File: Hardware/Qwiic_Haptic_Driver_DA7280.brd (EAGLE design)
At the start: 25.4 x 25.4 mm, 21 parts, among them J1 QWIIC_RIGHT_ANGLE, J2 QWIIC_RIGHT_ANGLE

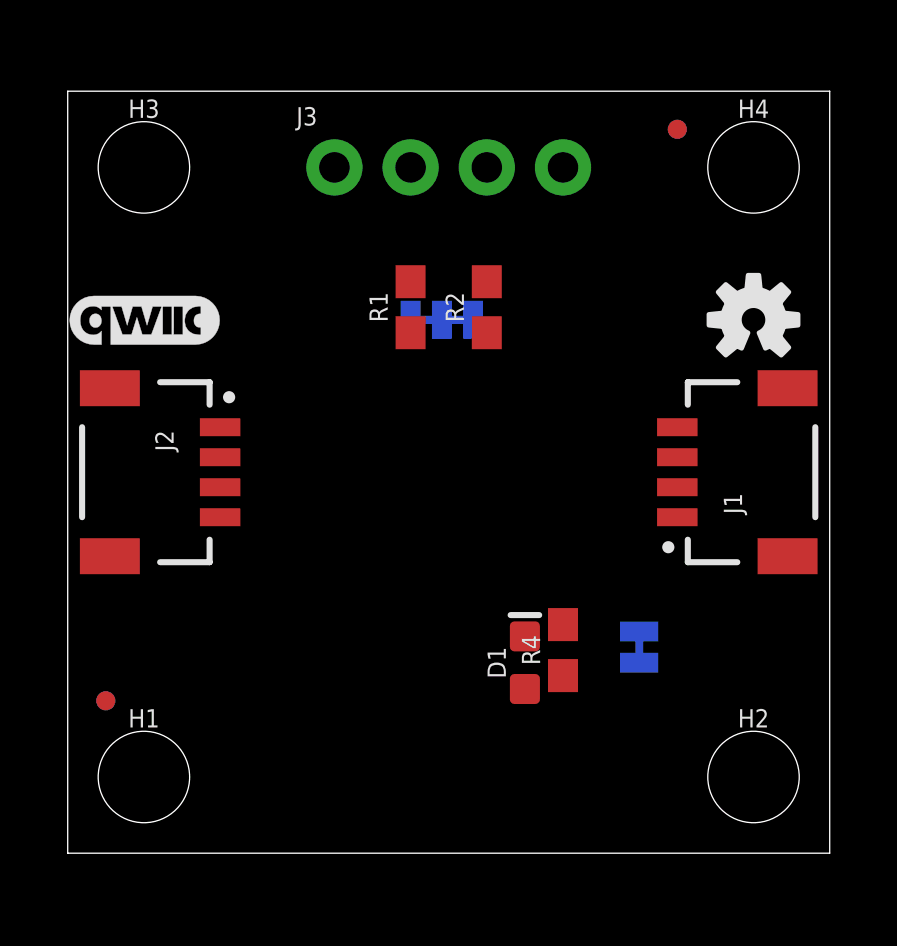
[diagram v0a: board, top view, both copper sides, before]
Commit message: Fully routed the board - still needs silk
Minor changes to the DA7280:
* symbol size was shortened.
* Footprint was centered at 0,0
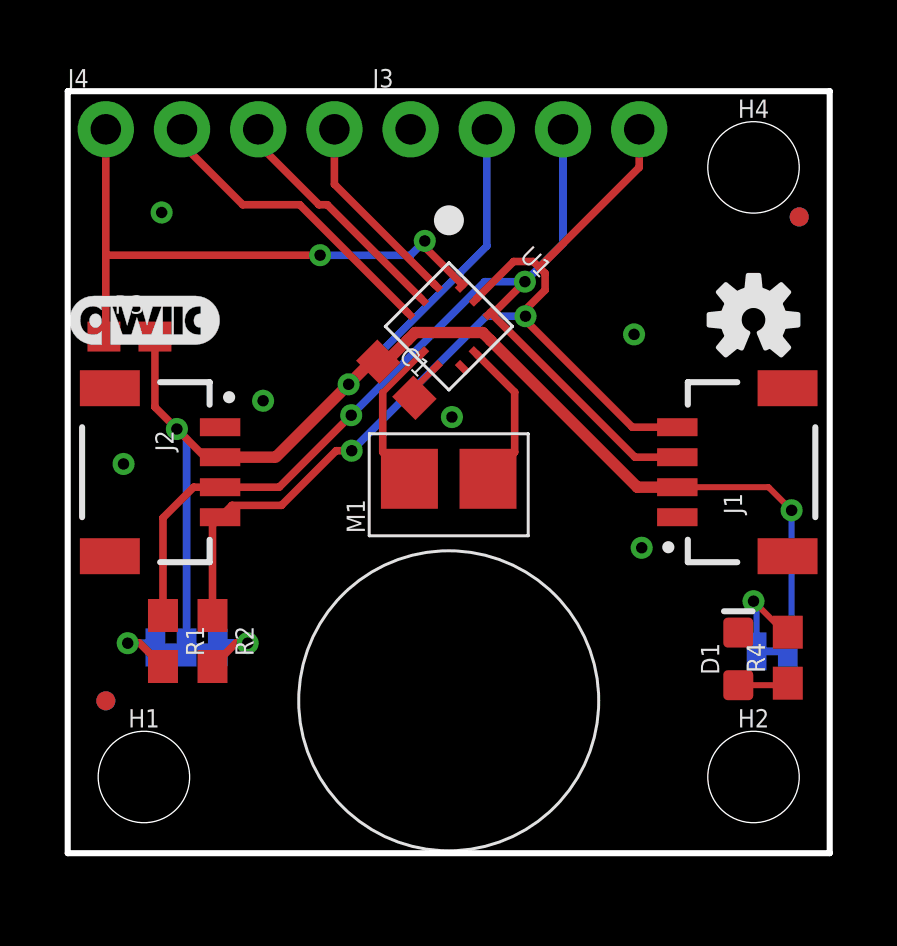
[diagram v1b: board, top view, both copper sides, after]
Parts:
- removed H3: STAND-OFFTIGHT, SparkFun-Hardware:STAND-OFF-TIGHT
- added C1: 0.1uF, SparkFun-Capacitors:0603
- added J4: (no value), SparkFun-Connectors:1X04_NO_SILK
- added M1: G1040003D_COIN_VIBRATION_MOTOR, TEMP:COIN_VIBRATION_MOTOR
- added R3: 10k, SparkFun-Resistors:0603
- added U1: HAPTIC_DRIVER_DA7280, TEMP:QFN_DA7280
- moved R2 14.4 mm to (4.83, 7.07), turned to 270 degrees
- moved R1 13.9 mm to (3.17, 7.07), turned to 270 degrees
- moved JP3 13.8 mm to (3.96, 6.86)
- moved R4 7.50 mm to (24.0, 6.52)
- moved D1 7.11 mm to (22.4, 6.48)
- moved FD1 5.00 mm to (24.4, 21.2)
- moved FD2 5.00 mm to (24.4, 21.2)
- moved JP1 4.43 mm to (23.5, 6.73), turned to 180 degrees
- moved J3 2.84 mm to (11.4, 24.1)
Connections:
- new net !INT!: J4.1, R3.1, U1.P12
- new net GPI0/PWM: J4.2, U1.P3
- new net GPI1: J4.3, U1.P2
- new net GPI2: J4.4, U1.P1
- new net N$5: M1.P$2, U1.P5
- new net N$6: M1.P$1, U1.P8
- net 3.3V: now also C1.1, R3.2, U1.P4, U1.P9
- net GND: now also C1.2, U1.P6, U1.P7
- net SCL: now also U1.P11
- net SDA: now also U1.P10
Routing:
- net 3.3V: track 0.00 -> 51.0 mm, vias 0 -> 3
- net SDA: track 0.00 -> 34.0 mm, vias 0 -> 2
- net SCL: track 0.00 -> 33.7 mm, vias 0 -> 2
- net !INT!: track 0.00 -> 19.8 mm, vias 0 -> 2
- net GPI0/PWM: track 0.00 -> 10.3 mm
- net GPI1: track 0.00 -> 8.07 mm
- net GPI2: track 0.00 -> 6.58 mm
- net N$5: track 0.00 -> 5.06 mm
- net N$6: track 0.00 -> 5.06 mm
- net N$2: track 0.00 -> 3.28 mm, vias 0 -> 1
- net N$4: track 0.00 -> 2.56 mm, vias 0 -> 1
- net N$3: track 0.00 -> 2.48 mm, vias 0 -> 1
- net N$1: track 0.00 -> 1.68 mm
- net GND: track 0.00 -> 1.29 mm, vias 0 -> 6
- added copper zone on layer 1, net GND
- added copper zone on layer 16, net GND

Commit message: Adds silk to PTH headers, cleans up schematic
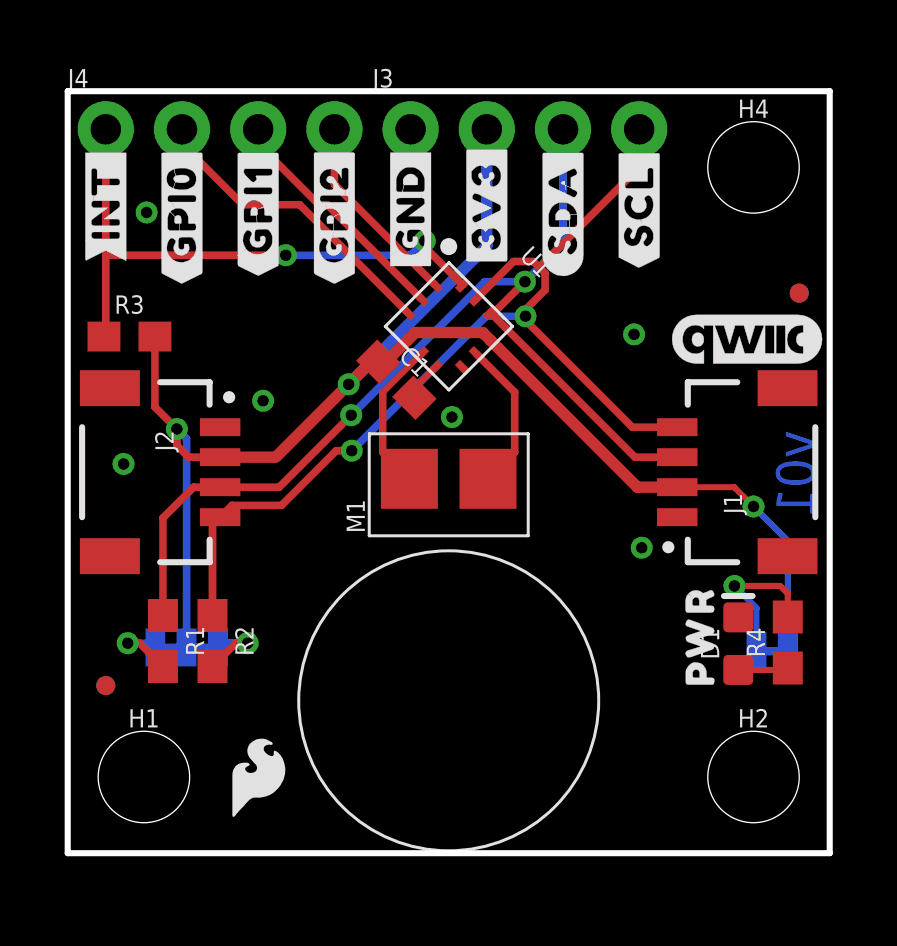
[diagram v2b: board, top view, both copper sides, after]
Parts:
- removed LOGO2: OSHW-LOGOS, SparkFun-Aesthetics:OSHW-LOGO-S
- added U$10: (no value), top:HAPTIC7
- added U$11: (no value), top:MOTOR_DRIVER8
- added U$12: (no value), bot:#GPI0#PWM#2
- added U$13: (no value), bot:#GPI1#2
- added U$14: (no value), bot:#GPI2#2
- added U$15: (no value), bot:#INT#3
- added U$16: (no value), bot:#SDA#0
- added U$17: (no value), SparkFun-Aesthetics:SFE_LOGO_FLAME_.1
- added U$18, U$3: (no value), top:#GND#0
- added U$19: (no value), top:#SCL#5
- added U$2, U$25: (no value), top:#3V3#1
- added U$20: (no value), top:PWR72810
- added U$21: (no value), bot:#SCL#1
- added U$22: (no value), SparkFun-Aesthetics:OSHW-LOGO-MINI
- added U$23: (no value), bot:#I2C#4
- added U$24: (no value), bot:#LED#4
- added U$4: (no value), top:#GPI0#6
- added U$5: (no value), top:#GPI1#6
- added U$6: (no value), top:#GPI2#6
- added U$7: (no value), top:#INT#6
- added U$8: (no value), top:#SDA#4
- added U$9: (no value), top:DA72809
- moved U$1 20.1 mm to (22.6, 17.1)
- moved FRAME1 5.68 mm to (-14.0, -12.7)
- moved FD1 2.54 mm to (24.4, 18.7)
- moved FD2 2.54 mm to (24.4, 18.7)
- moved LOGO1 2.36 mm to (15.0, 1.95)
- moved D1 0.51 mm to (22.4, 6.99)
- moved FD3 0.51 mm to (1.27, 5.59)
- moved FD4 0.51 mm to (1.27, 5.59)
- moved R4 0.51 mm to (24.0, 7.02)
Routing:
- net N$2: track 3.28 -> 5.15 mm
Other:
- board text added: "Elias Santistevan"
- board text added: "v01"

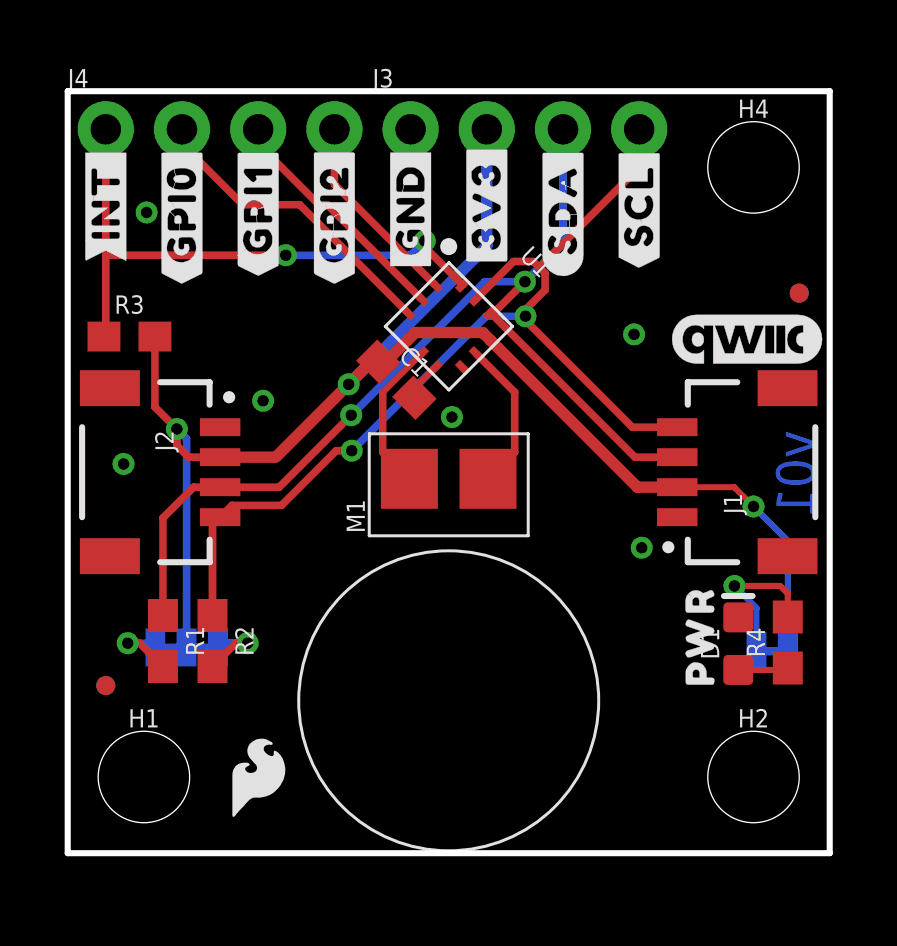
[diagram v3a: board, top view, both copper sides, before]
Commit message: Moves PTH interrupt closer to GND PTH hold and shifts all the GPI down.
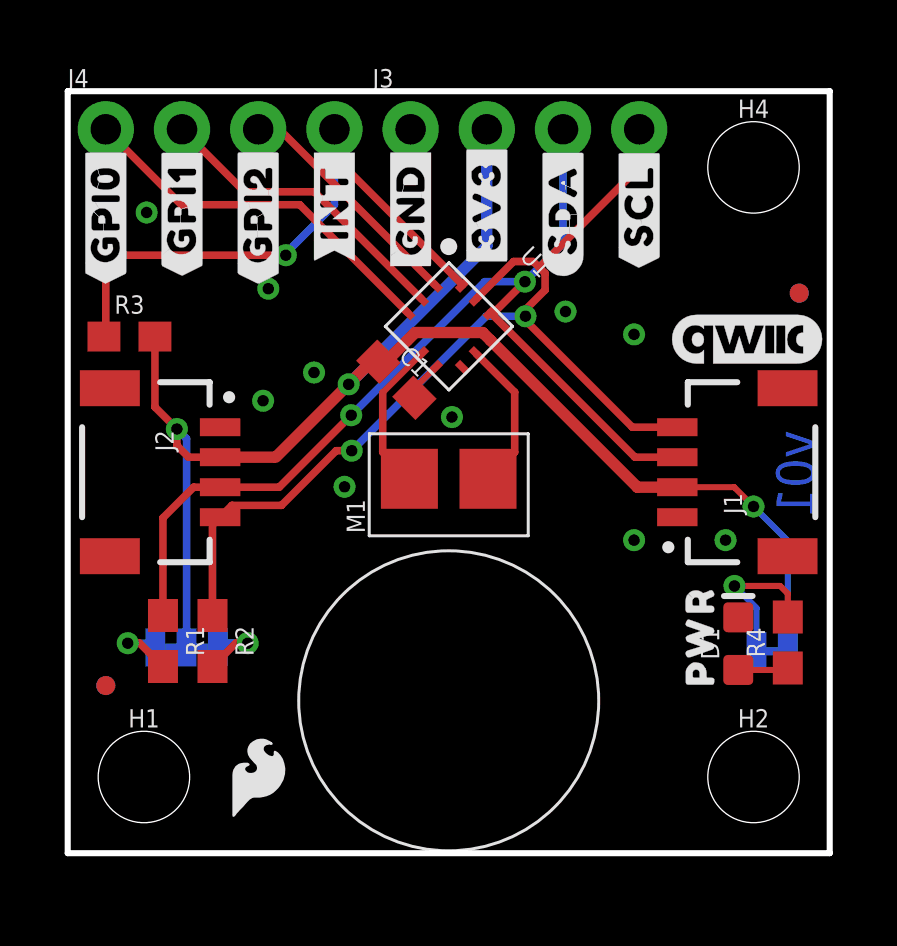
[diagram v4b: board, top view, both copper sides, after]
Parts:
- moved U$15 7.62 mm to (8.89, 21.7)
- moved U$7 7.62 mm to (8.89, 21.7)
- moved U$12 2.54 mm to (1.27, 19.1)
- moved U$14 2.54 mm to (6.35, 21.3)
- moved U$6 2.54 mm to (6.35, 21.3)
- moved U$4 2.54 mm to (1.27, 21.3)
- moved U$13 2.54 mm to (3.81, 21.5)
- moved U$5 2.54 mm to (3.81, 21.5)
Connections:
- net !INT!: now also J4.4; no longer J4.1
- net GPI0/PWM: now also J4.1; no longer J4.2
- net GPI1: now also J4.2; no longer J4.3
- net GPI2: now also J4.3; no longer J4.4
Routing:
- net GPI1: track 8.07 -> 10.3 mm
- net GPI0/PWM: track 10.3 -> 12.6 mm
- net GPI2: track 6.58 -> 8.05 mm
- net !INT!: track 19.8 -> 20.2 mm, vias 2 -> 1
- net GND: vias 6 -> 10
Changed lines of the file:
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@@
 <layer number="115" name="ReferenceISLANDS" color="7" fill="1" visible="no" active="no"/>
 <layer number="116" name="Patch_BOT" color="9" fill="4" visible="no" active="no"/>
-<layer number="117" name="PM_Ref" color="26" fill="1" visible="yes" active="yes"/>
+<layer number="117" name="PM_Ref" color="26" fill="1" visible="no" active="yes"/>
 <layer number="118" name="Rect_Pads" color="7" fill="1" visible="no" active="no"/>
-<layer number="119" name="PF_Ref" color="31" fill="1" visible="yes" active="yes"/>
-<layer number="120" name="WFL_Ref" color="25" fill="1" visible="yes" active="yes"/>
+<layer number="119" name="PF_Ref" color="31" fill="1" visible="no" active="yes"/>
+<layer number="120" name="WFL_Ref" color="25" fill="1" visible="no" active="yes"/>
 <layer number="121" name="_tsilk" color="7" fill="1" visible="no" active="no"/>
 <layer number="122" name="_bsilk" color="7" fill="1" visible="no" active="no"/>
@@
 </element>
 <element name="U$3" library="top" package="#GND#0" value="" x="11.43" y="21.463" smashed="yes" rot="R90"/>
-<element name="U$4" library="top" package="#GPI0#6" value="" x="3.81" y="21.336" smashed="yes" rot="R90"/>
-<element name="U$5" library="top" package="#GPI1#6" value="" x="6.35" y="21.463" smashed="yes" rot="R90"/>
-<element name="U$6" library="top" package="#GPI2#6" value="" x="8.89" y="21.336" smashed="yes" rot="R90"/>
-<element name="U$7" library="top" package="#INT#6" value="" x="1.27" y="21.717" smashed="yes" rot="R90"/>
+<element name="U$4" library="top" package="#GPI0#6" value="" x="1.27" y="21.336" smashed="yes" rot="R90"/>
+<element name="U$5" library="top" package="#GPI1#6" value="" x="3.81" y="21.463" smashed="yes" rot="R90"/>
+<element name="U$6" library="top" package="#GPI2#6" value="" x="6.35" y="21.336" smashed="yes" rot="R90"/>
+<element name="U$7" library="top" package="#INT#6" value="" x="8.89" y="21.717" smashed="yes" rot="R90"/>
 <element name="U$8" library="top" package="#SDA#4" value="" x="16.51" y="21.463" smashed="yes" rot="R90"/>
 <element name="U$9" library="top" package="DA72809" value="" x="12.573" y="14.859" smashed="yes" rot="MR0"/>
 <element name="U$10" library="top" package="HAPTIC7" value="" x="12.7" y="12.827" smashed="yes" rot="MR0"/>
 <element name="U$11" library="top" package="MOTOR_DRIVER8" value="" x="12.319" y="10.795" smashed="yes" rot="MR0"/>
-<element name="U$12" library="bot" package="#GPI0#PWM#2" value="" x="3.81" y="19.05" smashed="yes" rot="MR270"/>
-<element name="U$13" library="bot" package="#GPI1#2" value="" x="6.35" y="21.463" smashed="yes" rot="MR270"/>
-<element name="U$14" library="bot" package="#GPI2#2" value="" x="8.89" y="21.336" smashed="yes" rot="MR270"/>
-<element name="U$15" library="bot" package="#INT#3" value="" x="1.27" y="21.717" smashed="yes" rot="MR270"/>
+<element name="U$12" library="bot" package="#GPI0#PWM#2" value="" x="1.27" y="19.1008" smashed="yes" rot="MR270"/>
+<element name="U$13" library="bot" package="#GPI1#2" value="" x="3.81" y="21.463" smashed="yes" rot="MR270"/>
+<element name="U$14" library="bot" package="#GPI2#2" value="" x="6.35" y="21.336" smashed="yes" rot="MR270"/>
+<element name="U$15" library="bot" package="#INT#3" value="" x="8.89" y="21.717" smashed="yes" rot="MR270"/>
 <element name="U$16" library="bot" package="#SDA#0" value="" x="16.51" y="21.463" smashed="yes" rot="MR270"/>
 <element name="U$18" library="top" package="#GND#0" value="" x="11.43" y="21.463" smashed="yes" rot="MR270"/>
@@
 <wire x1="11.55564375" y1="15.490690625" x2="11.55564375" y2="15.180565625" width="0.2032" layer="1"/>
 <via x="6.513" y="15.081" extent="1-16" drill="0.381"/>
-<via x="19.133" y="10.181" extent="1-16" drill="0.381"/>
+<via x="21.927" y="10.435" extent="1-16" drill="0.381"/>
 <via x="18.879" y="17.293" extent="1-16" drill="0.381"/>
 <via x="2.631" y="21.357" extent="1-16" drill="0.381"/>
-<via x="1.861" y="12.975" extent="1-16" drill="0.381"/>
+<via x="16.593" y="18.055" extent="1-16" drill="0.381"/>
+<via x="8.211" y="16.023" extent="1-16" drill="0.381"/>
+<via x="9.227" y="12.213" extent="1-16" drill="0.381"/>
+<via x="6.687" y="18.817" extent="1-16" drill="0.381"/>
+<via x="18.879" y="10.435" extent="1-16" drill="0.381"/>
 </signal>
 <signal name="SCL">
@@
 <signal name="!INT!">
 <contactref element="U1" pad="P12"/>
-<contactref element="J4" pad="1"/>
 <contactref element="R3" pad="1"/>
-<wire x1="13.1666875" y1="18.9402125" x2="11.79985" y2="20.30705" width="0.254" layer="1"/>
-<wire x1="11.79985" y1="20.30705" x2="11.9022" y2="20.4094" width="0.254" layer="1"/>
-<via x="11.9022" y="20.4094" extent="1-16" drill="0.381"/>
-<wire x1="11.9022" y1="20.4094" x2="11.4228" y2="19.93" width="0.254" layer="16"/>
-<wire x1="11.4228" y1="19.93" x2="7.273075" y2="19.93" width="0.254" layer="16"/>
 <wire x1="7.2698375" y1="19.9332375" x2="7.273075" y2="19.93" width="0.254" layer="16"/>
 <via x="7.2698375" y="19.9332375" extent="1-16" drill="0.381"/>
-<wire x1="1.27" y1="24.13" x2="1.27" y2="19.9332375" width="0.254" layer="1"/>
-<wire x1="1.27" y1="19.9332375" x2="1.27" y2="17.2838" width="0.254" layer="1"/>
+<wire x1="1.27" y1="17.2838" x2="1.27" y2="19.304" width="0.254" layer="1"/>
 <wire x1="1.27" y1="17.2838" x2="1.2074" y2="17.2212" width="0.254" layer="1"/>
-<wire x1="7.2698375" y1="19.9332375" x2="1.27" y2="19.9332375" width="0.254" layer="1"/>
+<contactref element="J4" pad="4"/>
+<wire x1="13.1666875" y1="18.9402125" x2="8.89" y2="23.2169" width="0.254" layer="1"/>
+<wire x1="8.89" y1="23.2169" x2="8.89" y2="24.13" width="0.254" layer="1"/>
+<wire x1="1.27" y1="19.304" x2="1.8992375" y2="19.9332375" width="0.254" layer="1"/>
+<wire x1="1.8992375" y1="19.9332375" x2="7.2698375" y2="19.9332375" width="0.254" layer="1"/>
+<wire x1="7.2698375" y1="19.9332375" x2="7.2698375" y2="19.9952375" width="0.254" layer="16"/>
+<wire x1="8.89" y1="21.6154" x2="8.89" y2="24.13" width="0.254" layer="16"/>
+<wire x1="8.89" y1="21.6154" x2="7.2698375" y2="19.9952375" width="0.254" layer="16"/>
 </signal>
 <signal name="GPI1">
 <contactref element="U1" pad="P2"/>
-<contactref element="J4" pad="3"/>
-<wire x1="11.78783125" y1="18.48059375" x2="8.653025" y2="21.6154" width="0.254" layer="1"/>
-<wire x1="8.653025" y1="21.6154" x2="8.37446875" y2="21.6154" width="0.254" layer="1"/>
-<wire x1="6.35" y1="23.63986875" x2="6.35" y2="24.13" width="0.254" layer="1"/>
-<wire x1="8.37446875" y1="21.6154" x2="6.35" y2="23.63986875" width="0.254" layer="1"/>
+<contactref element="J4" pad="2"/>
+<wire x1="11.78783125" y1="18.48059375" x2="8.221225" y2="22.0472" width="0.254" layer="1"/>
+<wire x1="5.8928" y1="22.0472" x2="3.81" y2="24.13" width="0.254" layer="1"/>
+<wire x1="8.221225" y1="22.0472" x2="5.8928" y2="22.0472" width="0.254" layer="1"/>
 </signal>
 <signal name="GPI2">
 <contactref element="U1" pad="P1"/>
-<contactref element="J4" pad="4"/>
-<wire x1="12.24745" y1="18.9402125" x2="8.89" y2="22.2976625" width="0.254" layer="1"/>
-<wire x1="8.89" y1="22.2976625" x2="8.89" y2="24.13" width="0.254" layer="1"/>
+<contactref element="J4" pad="3"/>
+<wire x1="6.35" y1="24.13" x2="7.0576625" y2="24.13" width="0.254" layer="1"/>
+<wire x1="7.0576625" y1="24.13" x2="12.24745" y2="18.9402125" width="0.254" layer="1"/>
 </signal>
 <signal name="N$5">
@@
 </signal>
 <signal name="GPI0/PWM">
-<contactref element="J4" pad="2"/>
 <contactref element="U1" pad="P3"/>
 <wire x1="11.3282125" y1="18.020971875" x2="7.733784375" y2="21.6154" width="0.254" layer="1"/>
-<wire x1="7.733784375" y1="21.6154" x2="5.83446875" y2="21.6154" width="0.254" layer="1"/>
-<wire x1="3.81" y1="23.63986875" x2="3.81" y2="24.13" width="0.254" layer="1"/>
-<wire x1="5.83446875" y1="21.6154" x2="3.81" y2="23.63986875" width="0.254" layer="1"/>
+<contactref element="J4" pad="1"/>
+<wire x1="3.7846" y1="21.6154" x2="1.27" y2="24.13" width="0.254" layer="1"/>
+<wire x1="7.733784375" y1="21.6154" x2="3.7846" y2="21.6154" width="0.254" layer="1"/>
 </signal>
 </signals>
